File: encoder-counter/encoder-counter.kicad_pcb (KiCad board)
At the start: 4 copper layers, 65 x 40 mm, 15 parts, among them J1 530480910, J11 Conn_01x03, J12 Conn_01x03, J2 530480910, J3 530480910, J4 530480910, J5 530470610, Q1 DMG2305UX-13, Q2 DMG2305UX-13, U1 RaspberryPi_Pico_0, U2 RaspberryPi_Pico_0

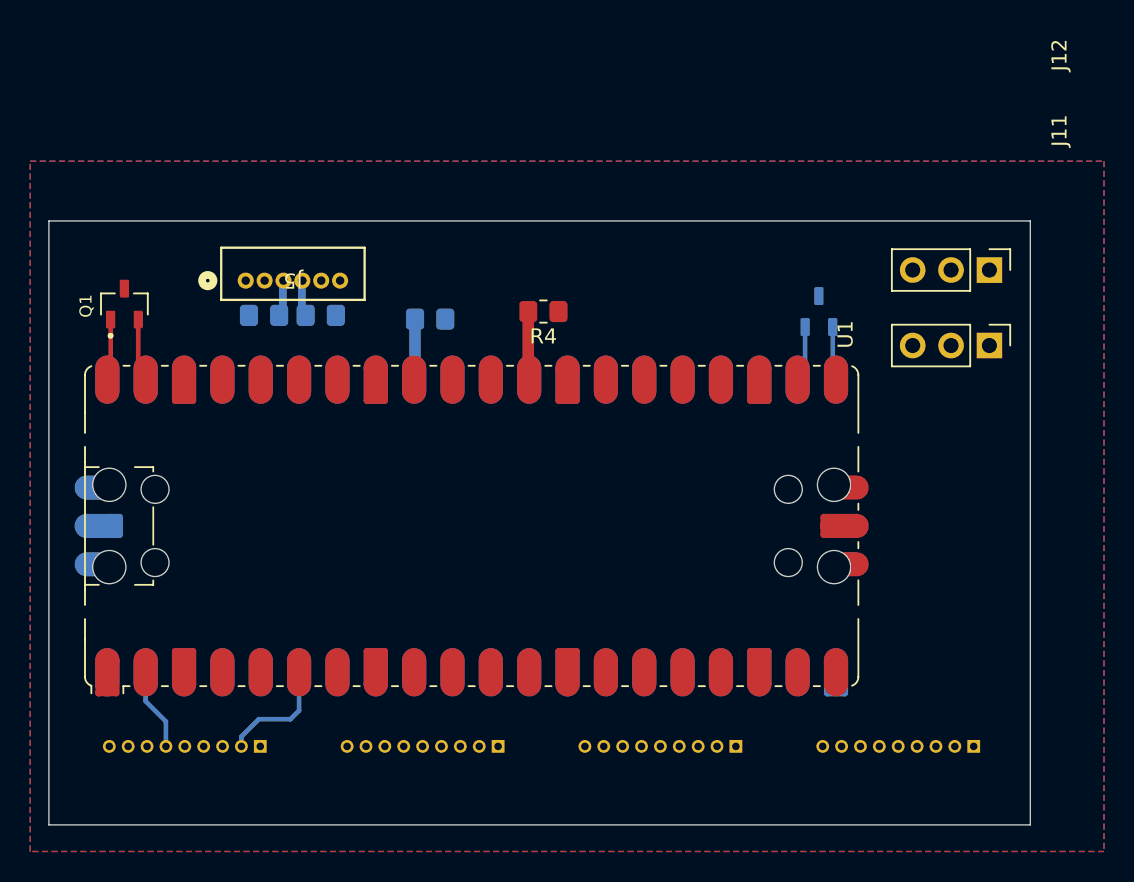
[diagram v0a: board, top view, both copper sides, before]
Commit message: First version of the layout. Libraries also updated. Step file added
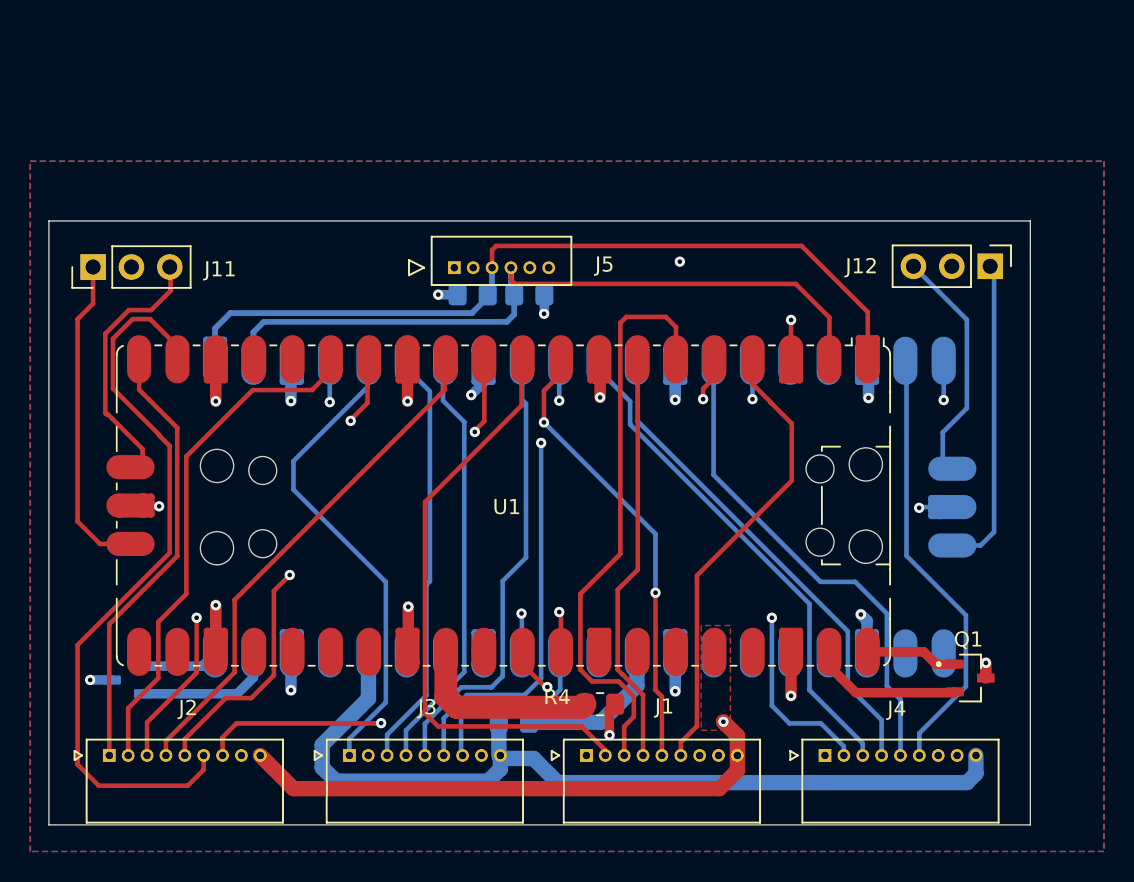
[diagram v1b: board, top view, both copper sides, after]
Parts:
- J1, J2, J3, J4: moved to F.Cu
- J5: footprint 530470610_6p:CONN06_530470610_MOL -> 6p_530470610:530470610
- moved Q1 61.3 mm to (174.0, 100.3), turned to 0 degrees
- moved J11 59.6 mm to (115.9, 73.1), turned to 90 degrees
- moved Q2 51.9 mm to (118.2, 100.4), turned to 180 degrees
- moved J2 41.5 mm to (117.0, 105.4), turned to 0 degrees
- moved J4 37.4 mm to (164.4, 105.4), turned to 0 degrees
- moved R3 27.3 mm to (143.8, 103.2), turned to 180 degrees
- moved R4 26.3 mm to (149.5, 102.0)
- moved J1 25.7 mm to (148.6, 105.4), turned to 0 degrees
- moved R1 13.9 mm to (144.8, 74.9)
- moved R2 13.9 mm to (141.1, 74.9)
- moved J5 13.8 mm to (139.9, 73.1)
- moved J3 9.87 mm to (132.9, 105.4), turned to 0 degrees
- moved U2 7.24 mm to (148.1, 89.0), turned to -90 degrees
- moved U1 2.50 mm to (143.1, 88.8), turned to -90 degrees
- moved J12 0.25 mm to (175.3, 73.0)
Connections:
- J5 pad 6: unconnected-(J5-Pin_6-Pad6) -> GND
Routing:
- net /5V: track 0.00 -> 105.8 mm, vias 0 -> 2
- net /pico0_3V3: track 0.00 -> 82.6 mm, vias 0 -> 3
- net /pico1_3V3: track 0.00 -> 57.3 mm
- net /I2C_SDA: track 2.42 -> 54.2 mm
- net /enc1_A: track 0.00 -> 49.0 mm
- net /I2C_SLC: track 2.42 -> 48.5 mm
- net /enc2_A: track 0.00 -> 43.5 mm, vias 0 -> 2
- net GND: track 0.00 -> 42.0 mm, vias 0 -> 18
- net /enc3_W/PWM: track 0.00 -> 41.3 mm, vias 0 -> 1
- net /enc0_miso: track 0.00 -> 39.7 mm
- net /enc1_miso: track 0.00 -> 39.5 mm, vias 0 -> 2
- net /enc0_mosi: track 0.00 -> 39.4 mm
- net /enc1_mosi: track 0.00 -> 34.1 mm
- net /enc1_CSN: track 0.00 -> 34.0 mm
- net /enc3_miso: track 0.00 -> 33.4 mm
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- added copper zone on F.Cu, net /pico0_3V3
